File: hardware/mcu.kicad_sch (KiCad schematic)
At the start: 55 parts, among them J10 PRPC004SAAN-RC, J6 SBH11-NBPC-D05-SM-BK, J7 PRPC006SAAN-RC, J8 PRPC001DAAN-RC, J9 PRPC006SAAN-RC, U4 AT25SF081B-SSHD-B, U5 MCP9808, U6 STM32L552CETx, Y1 ECS-160-9-37-CKM-TR3, Y2 ABS05-32.768KHZ-9-T

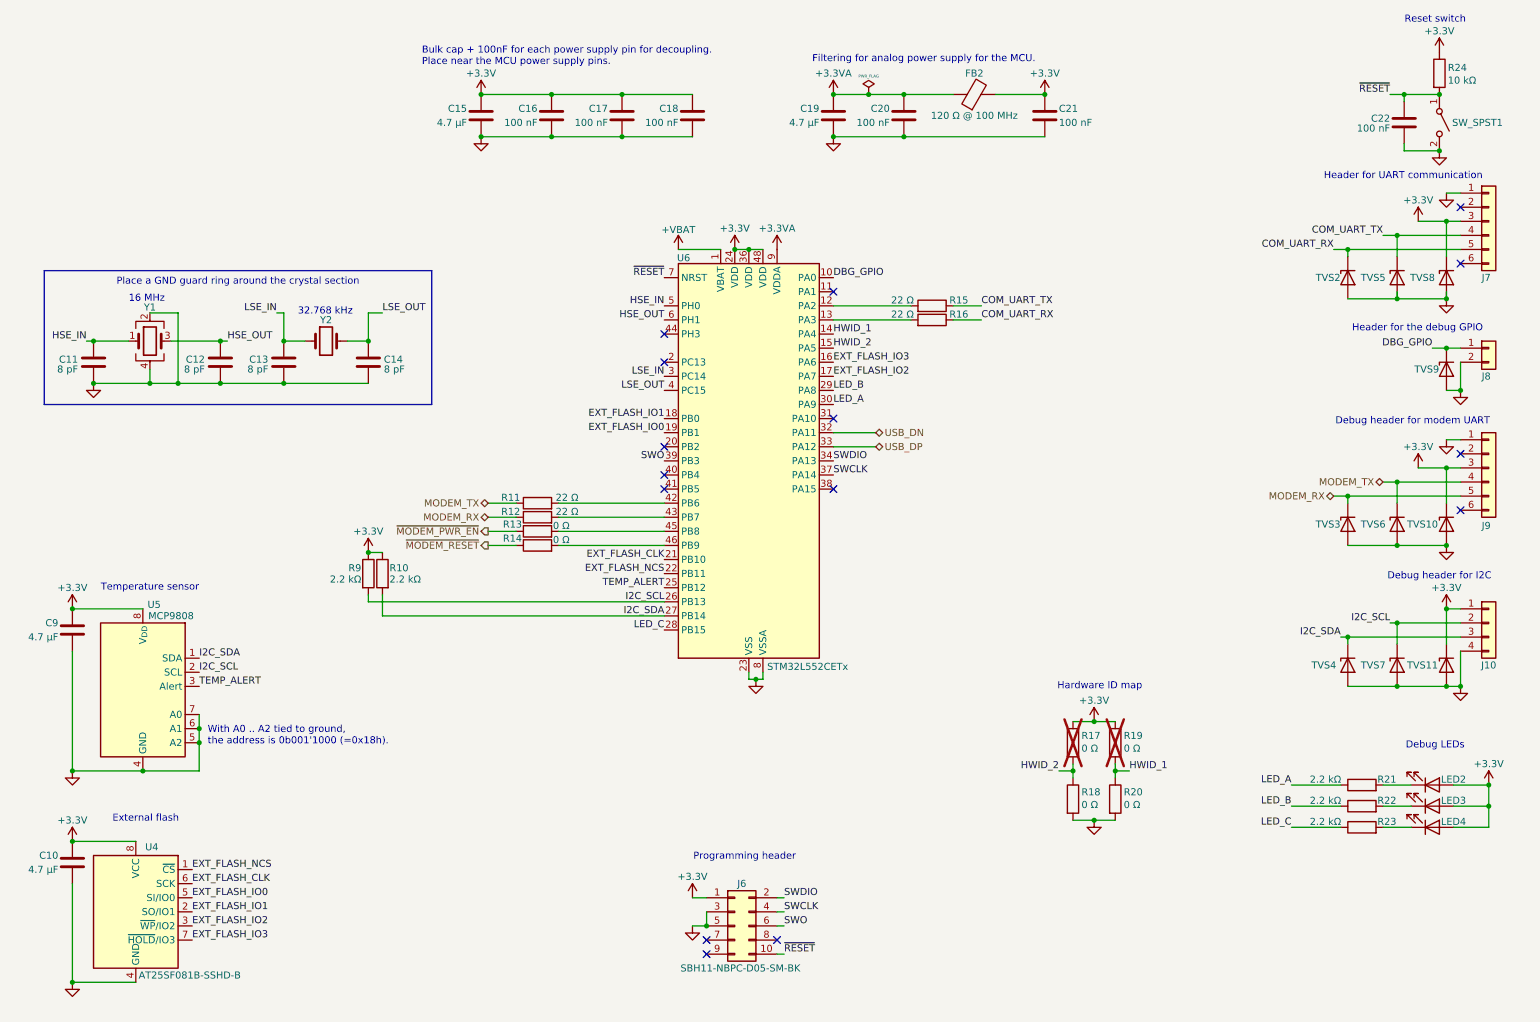
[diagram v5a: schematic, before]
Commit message: HW: Add battery protection
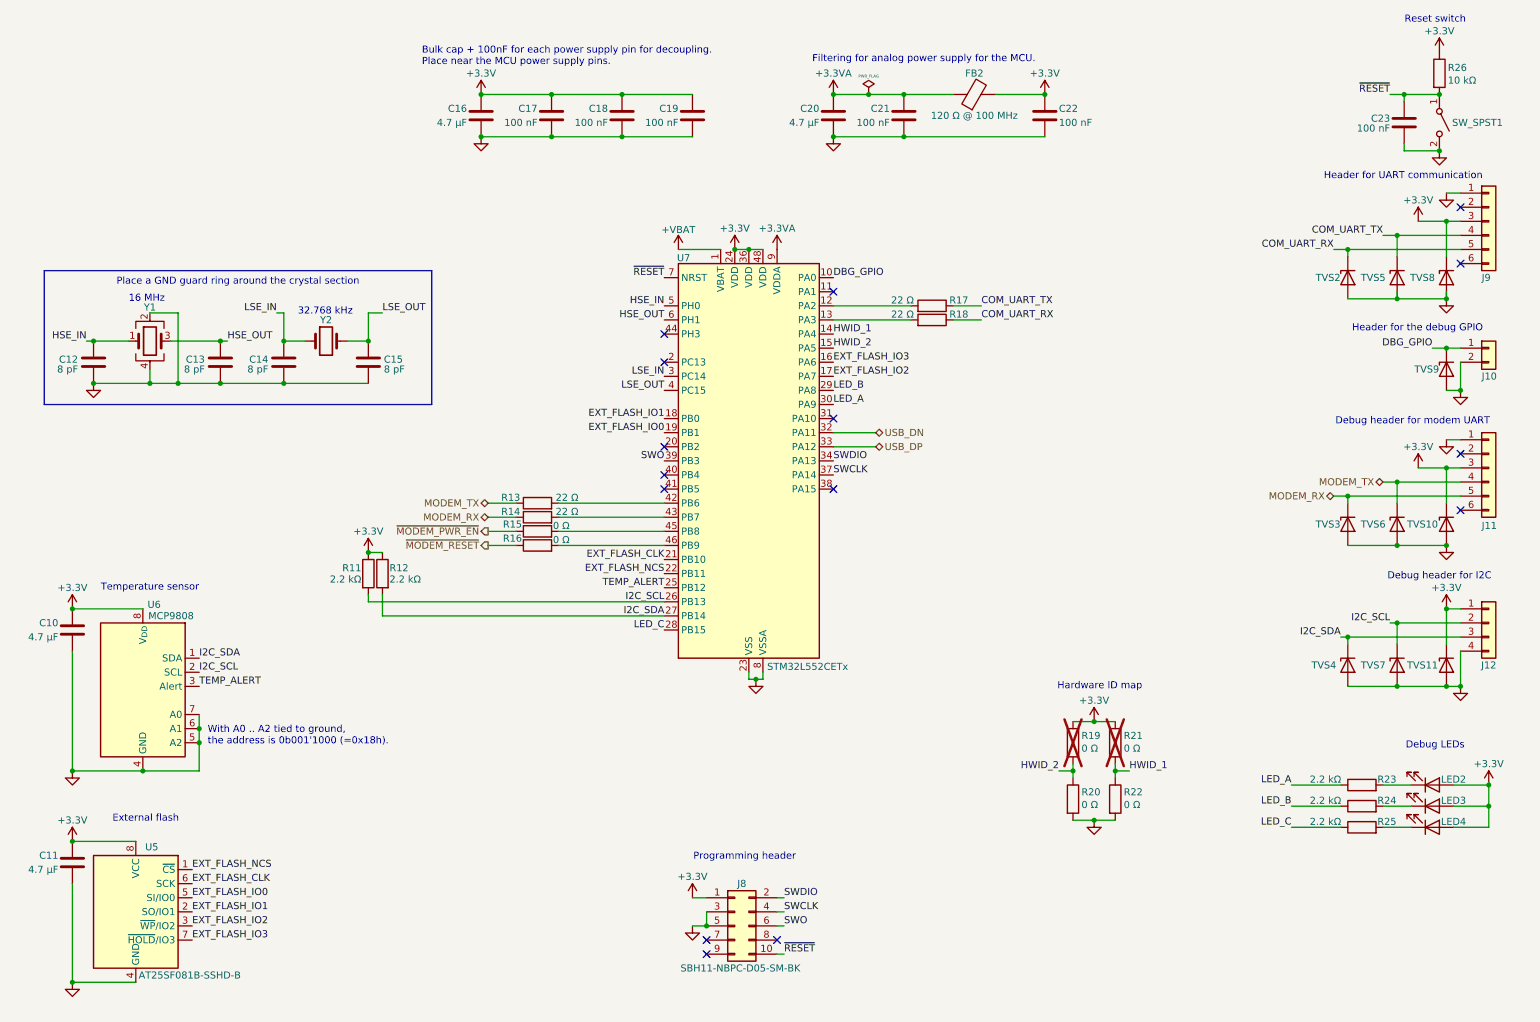
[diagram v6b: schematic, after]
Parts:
- renumbered C9 to C10, C10 to C11, C11 to C12, C12 to C13, C13 to C14, C14 to C15, C15 to C16, C16 to C17, C17 to C18, C18 to C19, C19 to C20, C20 to C21, C21 to C22, C22 to C23, J8 to J10, J9 to J11, J10 to J12, J6 to J8, J7 to J9, R9 to R11, R10 to R12, R11 to R13, R12 to R14, R13 to R15, R14 to R16, R15 to R17, R16 to R18, R17 to R19, R18 to R20, R19 to R21, R20 to R22, R21 to R23, R22 to R24, R23 to R25, R24 to R26, U4 to U5, U5 to U6, U6 to U7

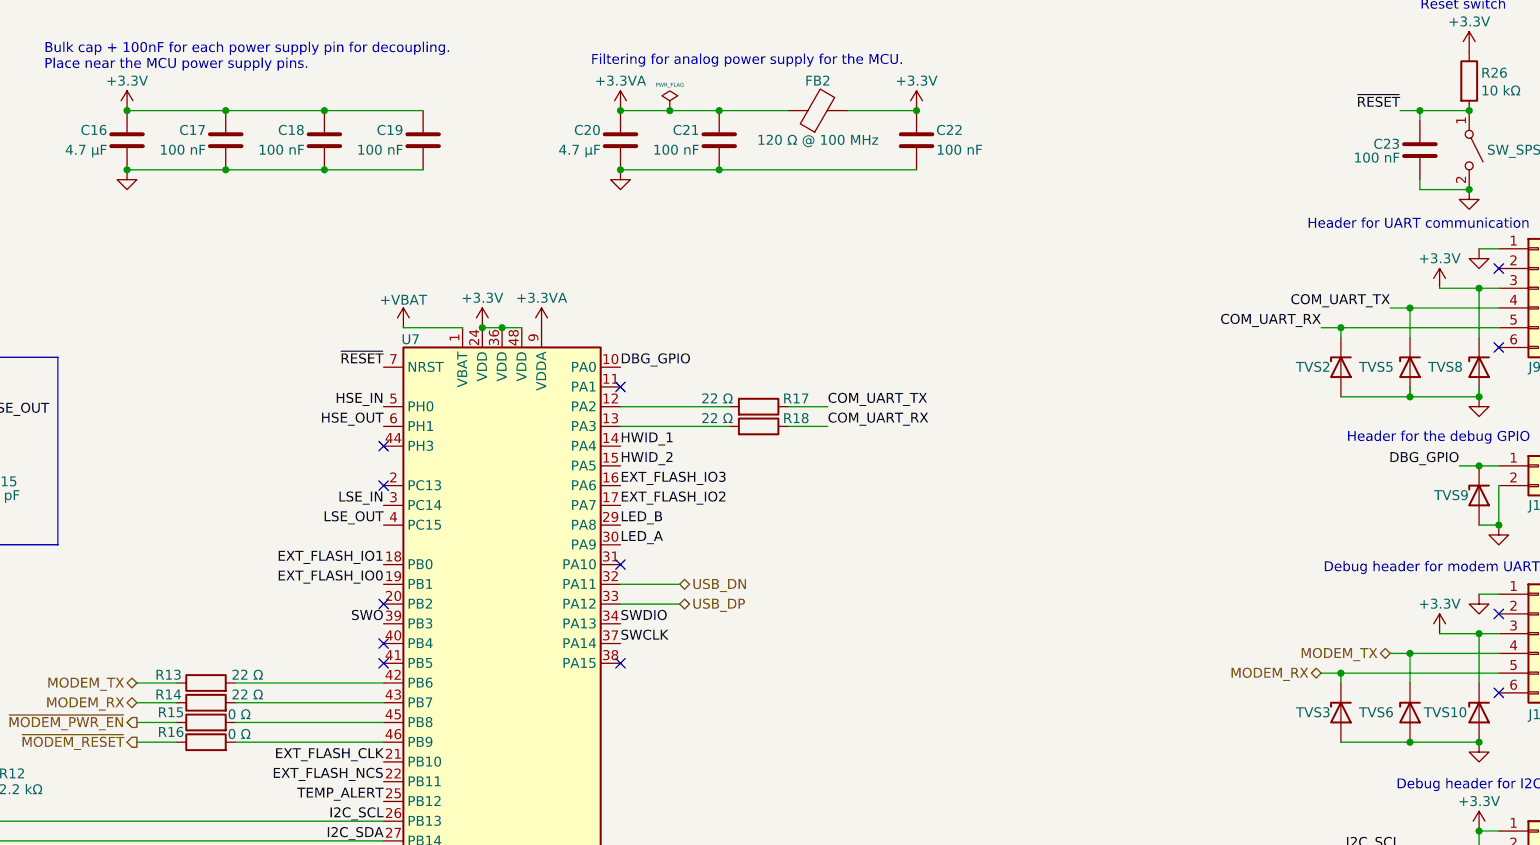
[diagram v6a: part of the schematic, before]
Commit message: HW: Replace 0402 with 0603 or bigger
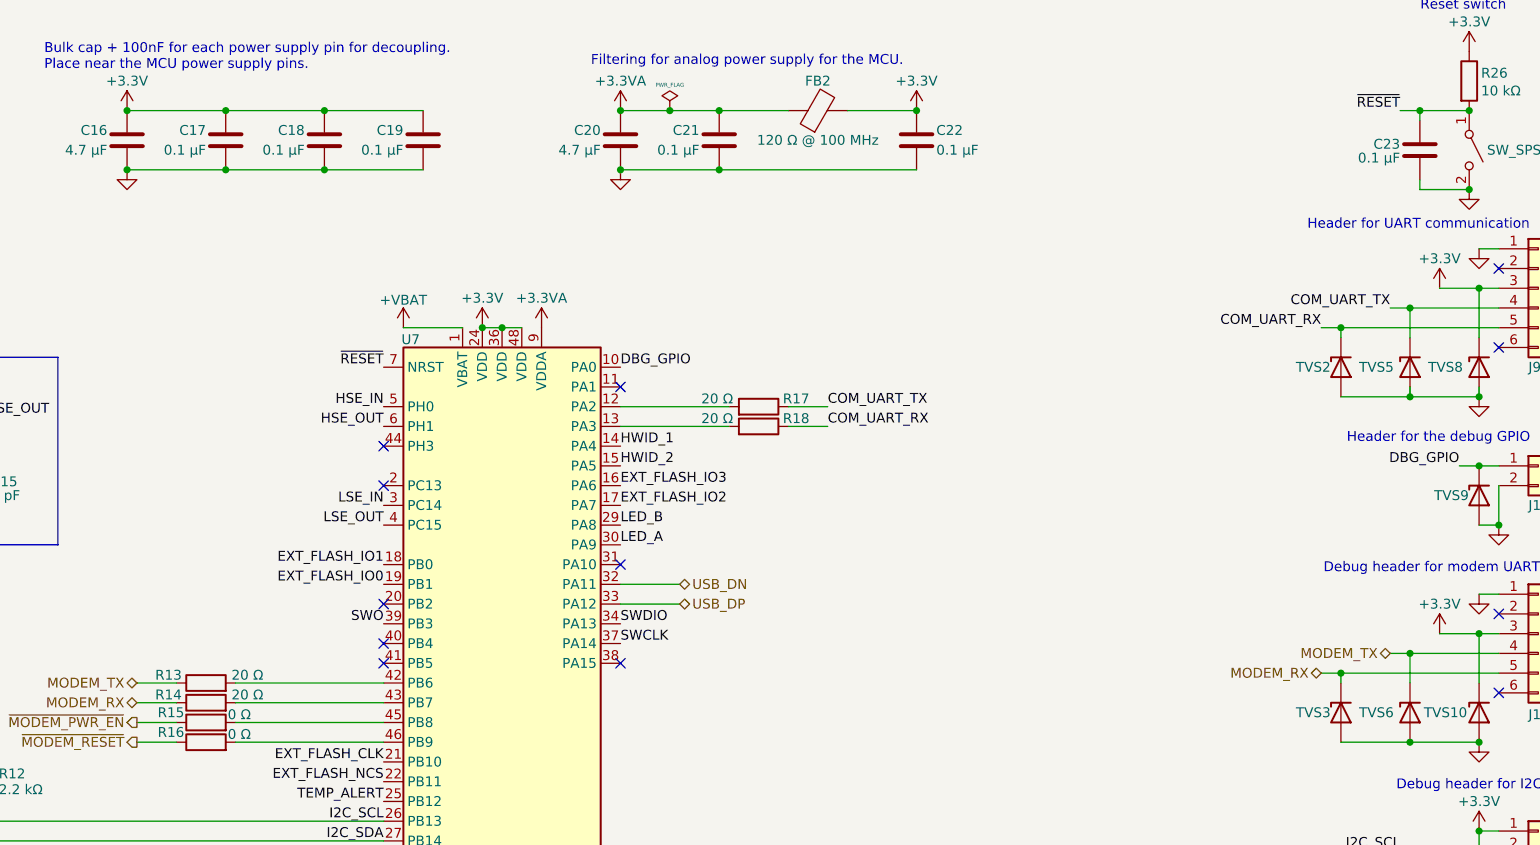
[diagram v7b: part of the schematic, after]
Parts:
- C10, C11, C16, C20: Digi-Key Part Number 1276-1044-1-ND -> 732-7902-1-ND; Manufacturer Samsung Electro-Mechanics -> Würth Elektronik; Manufacturer Part Number CL10A475KP8NNNC -> 885012106005
- C12, C13, C14, C15: footprint Capacitor_SMD:C_0402_1005Metric_Pad0.74x0.62mm_HandSolder -> Capacitor_SMD:C_0603_1608Metric_Pad1.08x0.95mm_HandSolder; Digi-Key Part Number 311-3708-1-ND -> 732-12050-1-ND; Manufacturer YAGEO -> Würth Elektronik; Manufacturer Part Number CC0402BRNPO9BN8R0 -> 885012006093
- C17, C18, C19, C21, C22, C23: value 100 nF -> 0.1 µF; footprint Capacitor_SMD:C_0402_1005Metric_Pad0.74x0.62mm_HandSolder -> Capacitor_SMD:C_0603_1608Metric_Pad1.08x0.95mm_HandSolder; Digi-Key Part Number 732-7513-1-ND -> 732-7989-1-ND; Manufacturer Part Number 885012205018 -> 885012206071
- R11, R12, R23, R24, R25: footprint Resistor_SMD:R_0402_1005Metric_Pad0.72x0.64mm_HandSolder -> Resistor_SMD:R_0603_1608Metric_Pad0.98x0.95mm_HandSolder; Digi-Key Part Number 732-560112110087CT-ND -> 732-560112116098CT-ND; Manufacturer Part Number 560112110087 -> 560112116098
- R13, R14, R17, R18: value 22 Ω -> 20 Ω; footprint Resistor_SMD:R_0402_1005Metric_Pad0.72x0.64mm_HandSolder -> Resistor_SMD:R_0603_1608Metric_Pad0.98x0.95mm_HandSolder; Digi-Key Part Number 732-560112110046CT-ND -> 732-560112116125CT-ND; Manufacturer Part Number 560112110046 -> 560112116125
- R15, R16, R19, R20, R21, R22: footprint Resistor_SMD:R_0402_1005Metric_Pad0.72x0.64mm_HandSolder -> Resistor_SMD:R_0805_2012Metric_Pad1.20x1.40mm_HandSolder; Digi-Key Part Number 732-560112110001CT-ND -> 732-560112120002CT-ND; Manufacturer Part Number 560112110001 -> 560112120002
- R26: footprint Resistor_SMD:R_0402_1005Metric_Pad0.72x0.64mm_HandSolder -> Resistor_SMD:R_0603_1608Metric_Pad0.98x0.95mm_HandSolder; Digi-Key Part Number 732-560112110020CT-ND -> 732-560112116005CT-ND; Manufacturer Part Number 560112110020 -> 560112116005
- TVS10, TVS11, TVS2, TVS3, TVS4, TVS5, TVS6, TVS7, TVS8, TVS9: value PE1605M1Q_R1_00001 -> SMAJ6.0CA-13-F; footprint Diode_SMD:D_0402_1005Metric_Pad0.77x0.64mm_HandSolder -> Diode_SMD:D_SMA_Handsoldering; Digi-Key Part Number 3757-PE1605M1Q_R1_00001CT-ND -> SMAJ6.0CA-13-FDICT-ND; Manufacturer Panjit International Inc. -> Diodes Incorporated; Manufacturer Part Number PE1605M1Q_R1_00001 -> SMAJ6.0CA-13-F

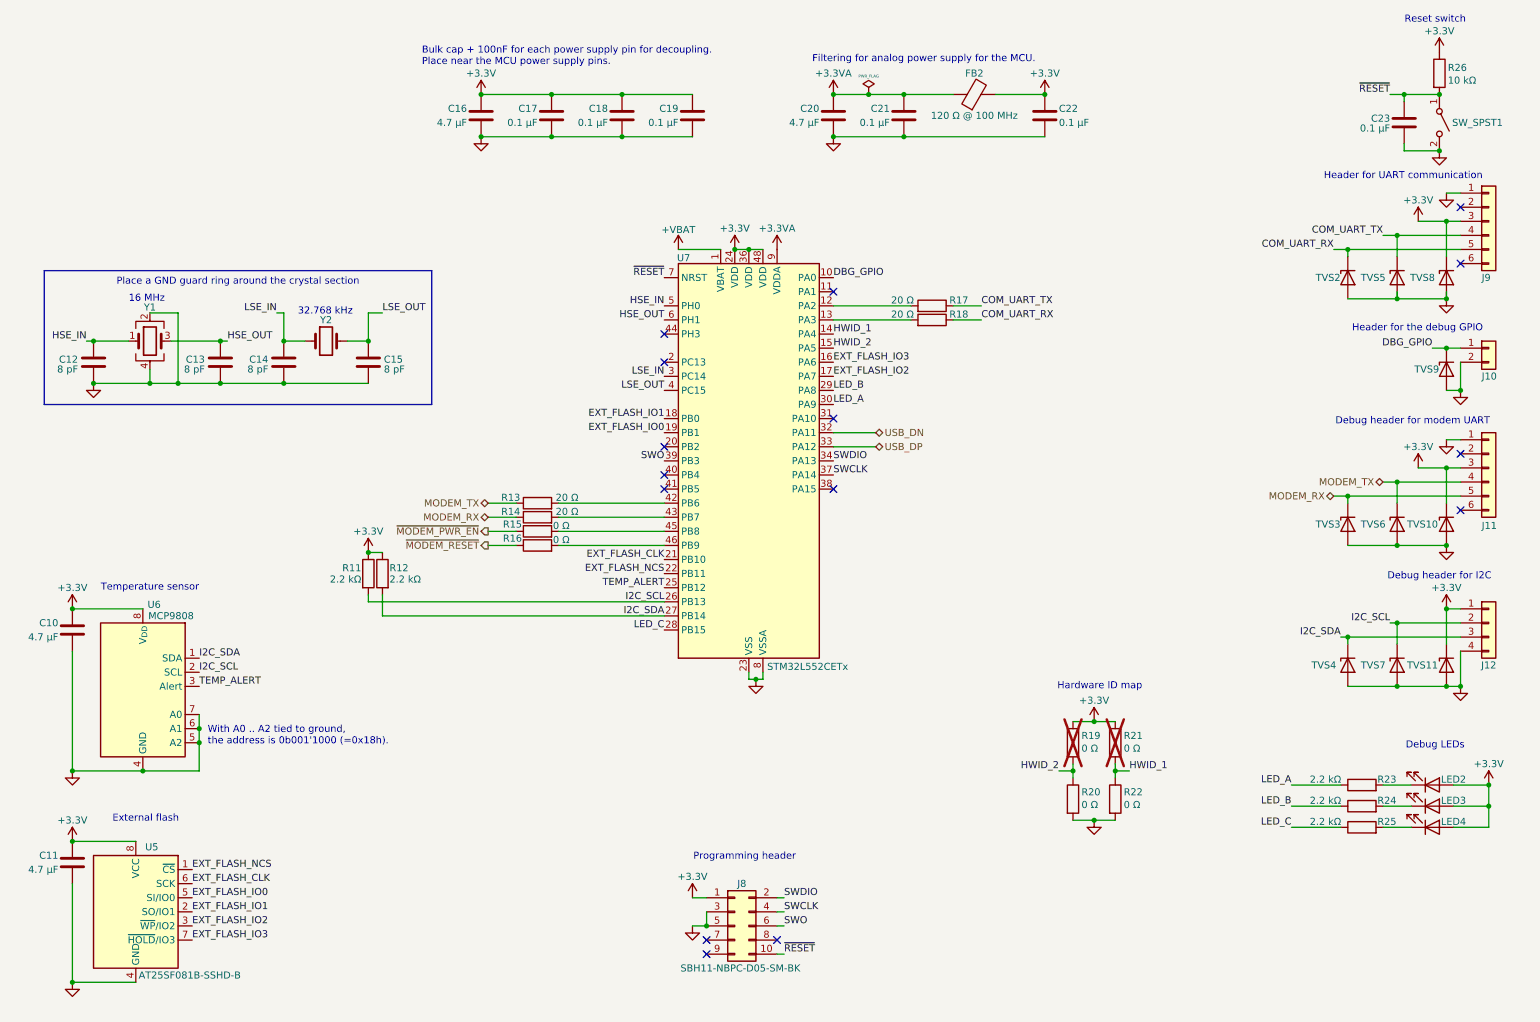
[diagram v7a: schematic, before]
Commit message: HW: Cleanup schematic
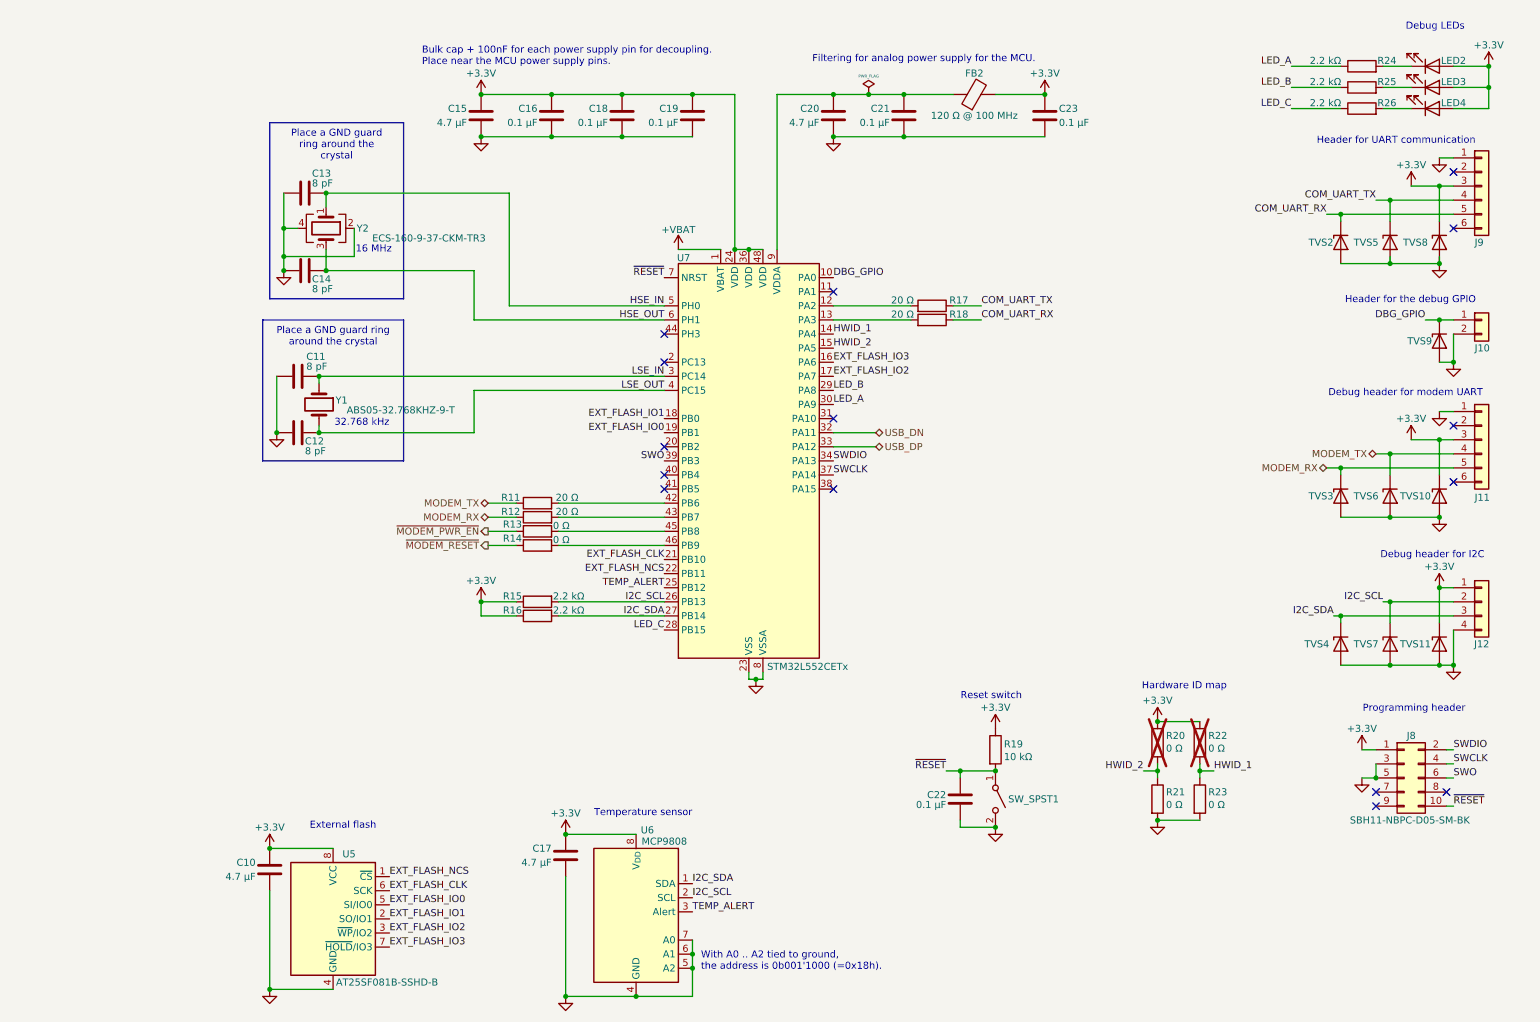
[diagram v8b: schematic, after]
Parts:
- removed R11: 2.2 kΩ, Resistor_SMD:R_0603_1608Metric_Pad0.98x0.95mm_HandSolder, symbol Device:R
- added R16: 2.2 kΩ, Resistor_SMD:R_0603_1608Metric_Pad0.98x0.95mm_HandSolder, symbol Device:R
- renumbered C11 to C10, C14 to C11, C15 to C12, C12 to C13, C13 to C14, C16 to C15, C17 to C16, C10 to C17, C23 to C22, C22 to C23, R13 to R11, R14 to R12, R15 to R13, R16 to R14, R12 to R15, R26 to R19, R19 to R20, R20 to R21, R21 to R22, R22 to R23, R23 to R24, R24 to R25, R25 to R26, Y2 to Y1, Y1 to Y2
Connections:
- net +3.3V: now also R16.1
- net I2C_SCL: now also R15.2
- net I2C_SDA: now also R16.2; no longer R15.2
- net +3.3VA: no longer names the net of C20.1, C21.1, FB2.1, U7.9 (VDDA)
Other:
- moved on the sheet: C10, C11, C12, C13, C14, C17, C22, J10, J11, J12, J8, J9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
